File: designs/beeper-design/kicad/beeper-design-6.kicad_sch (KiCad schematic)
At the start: 24 parts, among them U13 CSD75207W15, U3 BQ51003YFPR, U5 FH19C-6S-0.5SH(10)

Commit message: another export
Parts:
- removed C14: 2.2u, beeper-design:Pkg0201_25, symbol my_capacitor_7
- removed C15: 470n, beeper-design:Pkg0201_21, symbol my_capacitor_5
- removed C16: 470n, beeper-design:Pkg0201_31, symbol my_capacitor_10
- removed C17: 22n, beeper-design:Pkg0201_45, symbol my_capacitor_18
- removed C18: 22n, beeper-design:Pkg0201_9, symbol my_capacitor_2
- removed C19: 10n, beeper-design:Pkg0201_18, symbol my_capacitor_4
- removed C20: 10n, beeper-design:Pkg0201_30, symbol my_capacitor_9
- removed C21: 270p, beeper-design:Pkg0201_43, symbol my_capacitor_16
- removed C22: 10n, beeper-design:Pkg0201_7, symbol my_capacitor
- removed C23: 10u, beeper-design:Pkg0402_2, symbol C105225_2
- removed C24: 4.7u, beeper-design:Pkg0402_6, symbol C23733_1
- removed C25: 4.7u, beeper-design:Pkg0402_4, symbol C23733
- removed R2: 845R, beeper-design:Pkg0201_36, symbol my_resistor_10
- removed R3: 196R, beeper-design:Pkg0201_2, symbol C138167
- removed R4: 20K, beeper-design:Pkg0201_12, symbol my_resistor_3
- removed R5: 10K, beeper-design:Pkg0201_22, symbol my_resistor_7
- removed R6: 10K, beeper-design:Pkg0201_34, symbol my_resistor_9
- removed R7: 10K, beeper-design:Pkg0201, symbol my_resistor_12
- removed R8: 1K, beeper-design:Pkg0201_11, symbol my_resistor_2
- removed U13: CSD75207W15, beeper-design:LP_6, symbol CSD75207W15
- added C14: 2.2u, beeper-design:Pkg0201_2, symbol C335106
- added C15: 2.2u, beeper-design:Pkg0201_51, symbol C335106_35
- added C16: 2.2u, beeper-design:Pkg0201_12, symbol C335106_10
- added C17: 2.2u, beeper-design:Pkg0201_25, symbol C335106_18
- added C18: 2.2u, beeper-design:Pkg0201_37, symbol C335106_26
- added C19: 2.2u, beeper-design:Pkg0201_49, symbol C335106_33
- added C20: 2.2u, beeper-design:Pkg0201_10, symbol C335106_8
- added C21: 2.2u, beeper-design:Pkg0201_23, symbol C335106_16
- added C22: 2.2u, beeper-design:Pkg0201_35, symbol C335106_25
- added C23: 2.2u, beeper-design:Pkg0201_48, symbol C335106_32
- added C24: 2.2u, beeper-design:Pkg0201_7, symbol C335106_5
- added C25: 2.2u, beeper-design:Pkg0201_22, symbol C335106_15
- added R2: 845R, beeper-design:Pkg0201_15, symbol my_resistor_1
- added R3: 10K, beeper-design:Pkg0201_14, symbol my_resistor
- added R4: 20K, beeper-design:Pkg0201_41, symbol my_resistor_10
- added R5: 10K, beeper-design:Pkg0201, symbol my_resistor_14
- added R6: 196R, beeper-design:Pkg0201_28, symbol C138167
- added R7: 10K, beeper-design:Pkg0201_26, symbol my_resistor_5
- added R8: 1K, beeper-design:Pkg0201_38, symbol my_resistor_8
- U3: footprint beeper-design:LP_7 -> beeper-design:LP_6
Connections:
- net VDD1P8 is gone; now on net VBUS: U3.D1 (OUT), U3.D2 (OUT), U3.D3 (OUT), U3.D4 (OUT)
- net GND: now also C14.1, C23.1, C24.1, C25.1, R3.2, R5.2, R6.2, R7.2, R8.2
- net VBUS: now also C14.2, C25.2
- net mcu_mcu-wpwr0_gpio: now also R5.1
- net mcu_mcu-wpwr1_gpio: now also R3.1
- net mcu_mcu-wpwr3_gpio: now also R7.1
- net at U3.B3 (AC1), U3.B4 (AC1): now also C15.1, C17.1, C19.1, C21.2, C22.2
- net at U3.C4 (BOOT1): now also C19.2
- net at TP14.p, U3.B1 (AC2), U3.B2 (AC2): now also C16.1, C18.1, C20.1, C21.1
- net at U3.C1 (BOOT2): now also C20.2
- net at U3.C2 (RECT), U3.C3 (RECT): now also C23.2, C24.2, R4.2
- net at U3.G1 (ILIM): now also R2.1
- net at U3.F2 (FOD): now also R2.2, R4.1, R6.1
- net at U3.E3 (CLAMP1): now also C15.2
- net at U3.E1 (COMM2): now also C18.2
- net at U3.E2 (CLAMP2): now also C16.2
- net at U3.E4 (COMM1): now also C17.2
- net at U3.G4 (AD): now also R8.1
- net at TP13.p: now also C22.1

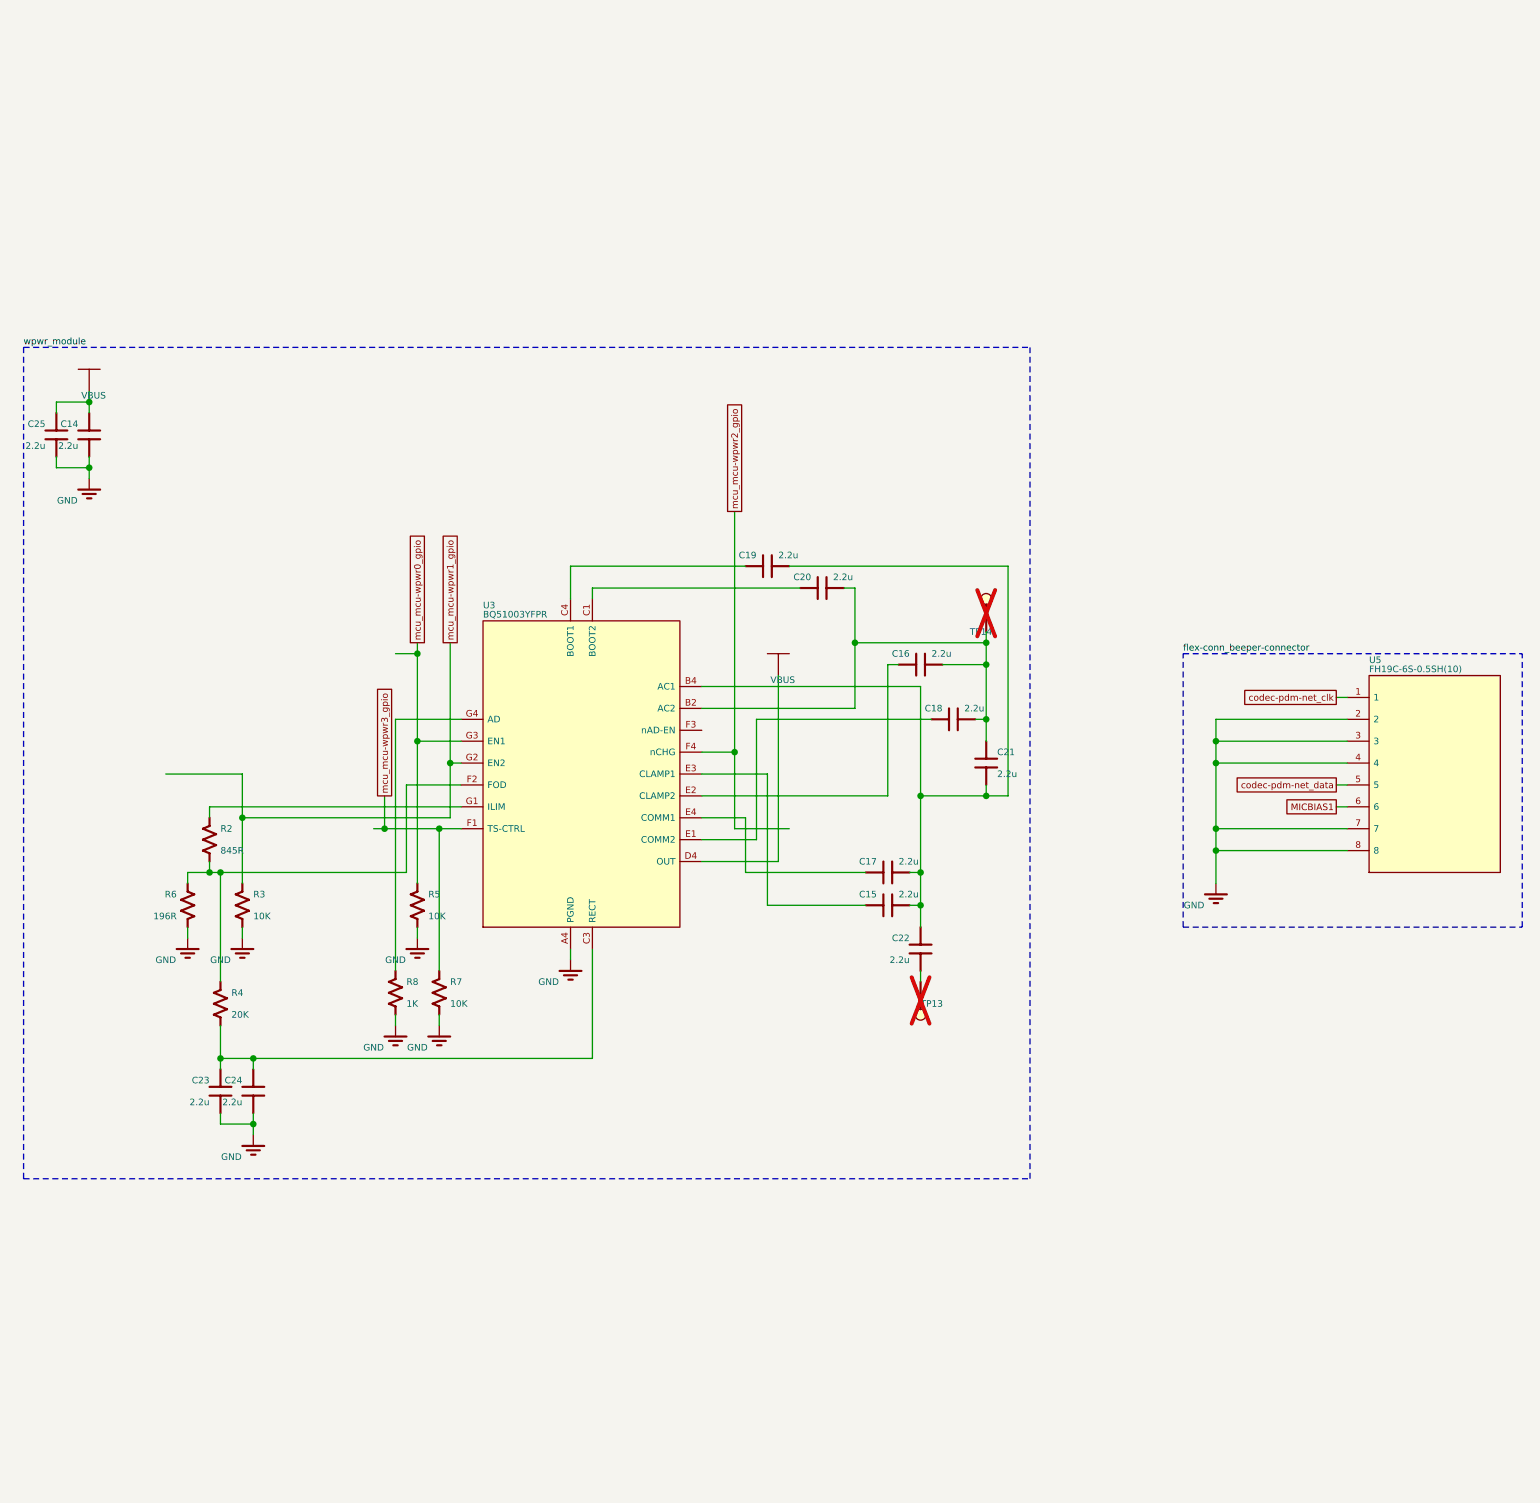
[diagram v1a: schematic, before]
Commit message: crash with new usb connector
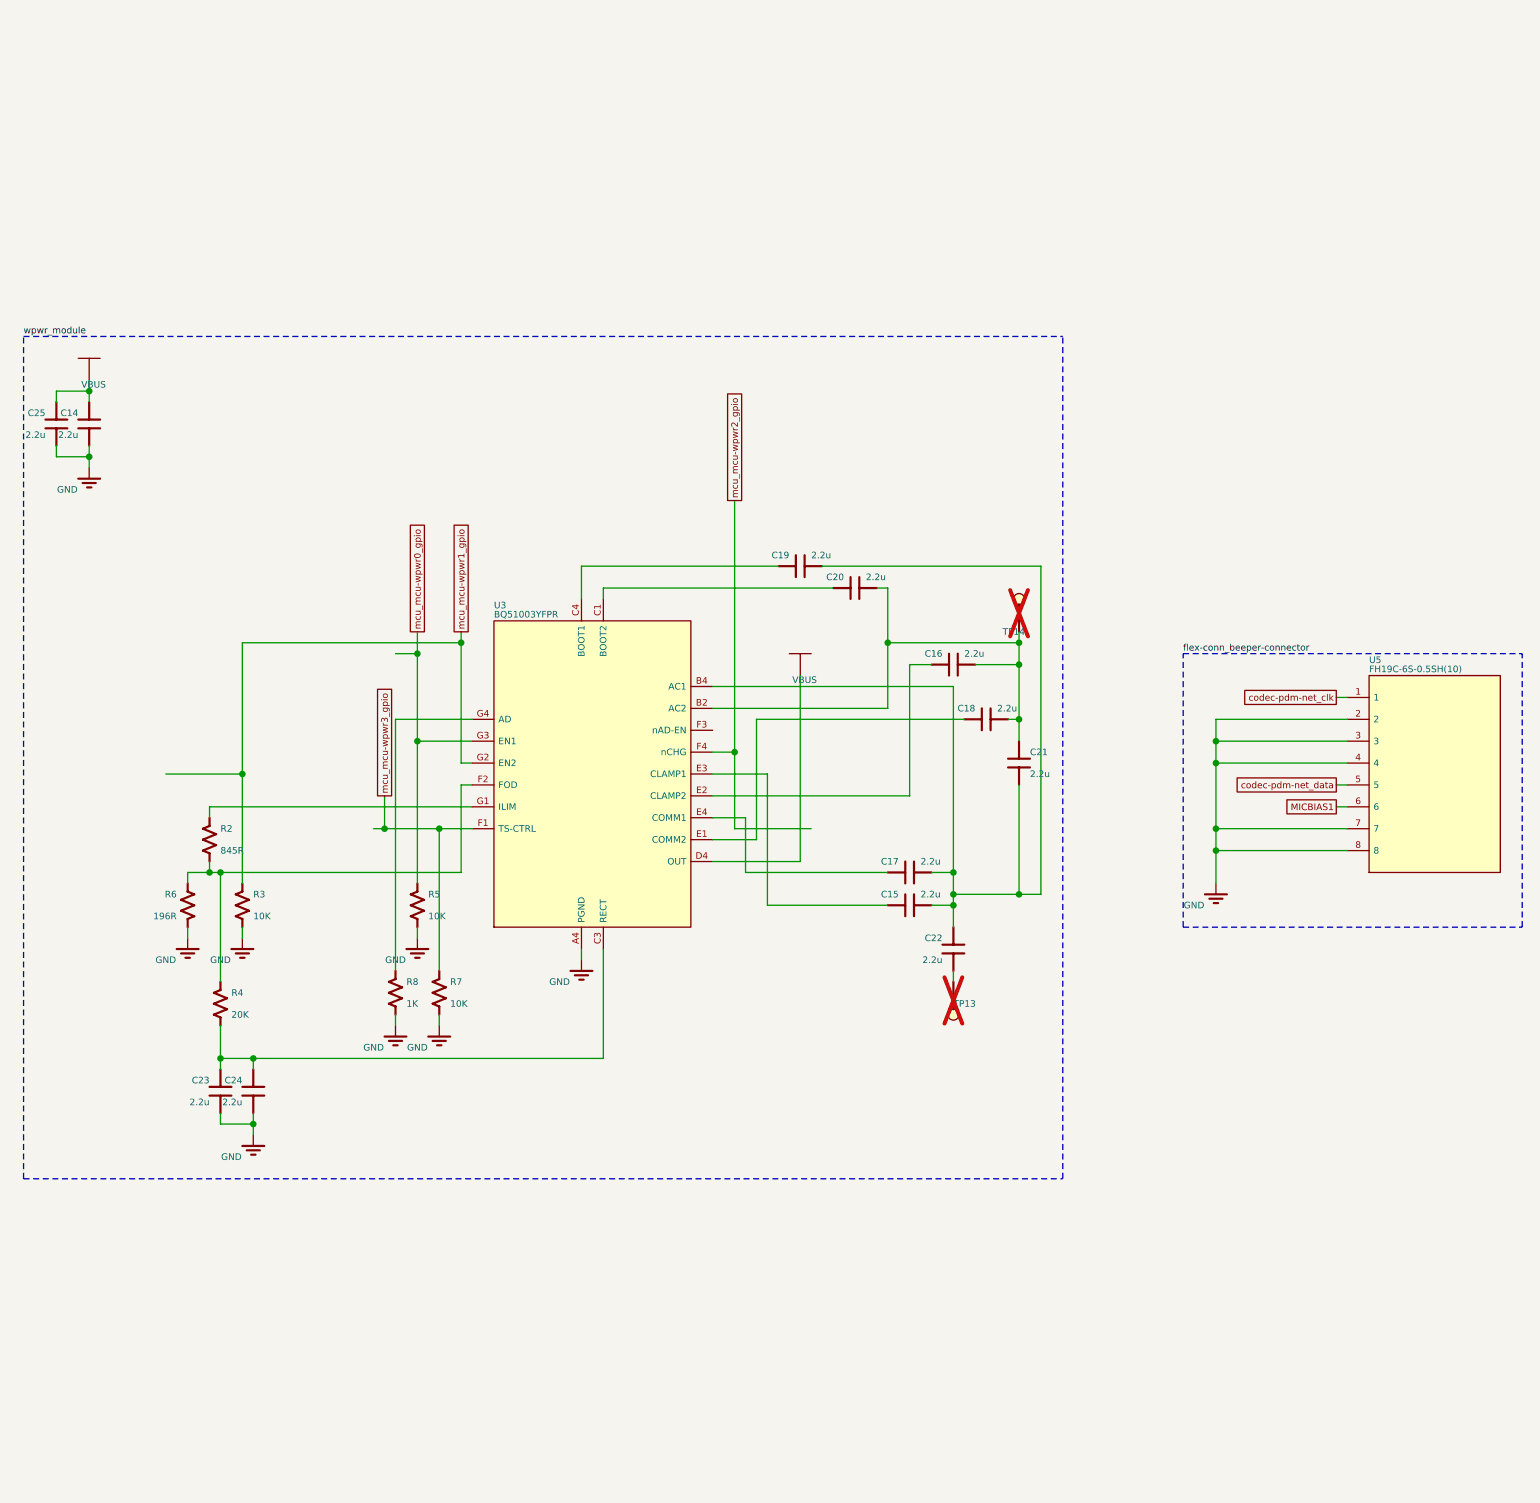
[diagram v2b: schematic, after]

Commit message: new export
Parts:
- removed C14: 2.2u, beeper-design:Pkg0201_2, symbol C335106
- removed C15: 2.2u, beeper-design:Pkg0201_51, symbol C335106_35
- removed C16: 2.2u, beeper-design:Pkg0201_12, symbol C335106_10
- removed C17: 2.2u, beeper-design:Pkg0201_25, symbol C335106_18
- removed C18: 2.2u, beeper-design:Pkg0201_37, symbol C335106_26
- removed C19: 2.2u, beeper-design:Pkg0201_49, symbol C335106_33
- removed C20: 2.2u, beeper-design:Pkg0201_10, symbol C335106_8
- removed C21: 2.2u, beeper-design:Pkg0201_23, symbol C335106_16
- removed C22: 2.2u, beeper-design:Pkg0201_35, symbol C335106_25
- removed C23: 2.2u, beeper-design:Pkg0201_48, symbol C335106_32
- removed C24: 2.2u, beeper-design:Pkg0201_7, symbol C335106_5
- removed C25: 2.2u, beeper-design:Pkg0201_22, symbol C335106_15
- removed R2: 845R, beeper-design:Pkg0201_15, symbol my_resistor_1
- removed R4: 20K, beeper-design:Pkg0201_41, symbol my_resistor_10
- removed R7: 10K, beeper-design:Pkg0201_26, symbol my_resistor_5
- removed R8: 1K, beeper-design:Pkg0201_38, symbol my_resistor_8
- added C14: 2.2u, beeper-design:Pkg0201, symbol C335106_35
- added C15: 2.2u, beeper-design:Pkg0201_50, symbol C335106_31
- added C16: 2.2u, beeper-design:Pkg0201_9, symbol C335106_7
- added C17: 2.2u, beeper-design:Pkg0201_22, symbol C335106_14
- added C18: 2.2u, beeper-design:Pkg0201_36, symbol C335106_22
- added C19: 2.2u, beeper-design:Pkg0201_49, symbol C335106_30
- added C20: 2.2u, beeper-design:Pkg0201_7, symbol C335106_5
- added C21: 2.2u, beeper-design:Pkg0201_20, symbol C335106_12
- added C22: 2.2u, beeper-design:Pkg0201_33, symbol C335106_20
- added C23: 2.2u, beeper-design:Pkg0201_48, symbol C335106_29
- added C24: 2.2u, beeper-design:Pkg0201_6, symbol C335106_4
- added C25: 2.2u, beeper-design:Pkg0201_18, symbol C335106_11
- added R2: 845R, beeper-design:Pkg0201_15, symbol my_resistor_3
- added R4: 20K, beeper-design:Pkg0201_40, symbol my_resistor_11
- added R7: 10K, beeper-design:Pkg0201_23, symbol my_resistor_6
- added R8: 1K, beeper-design:Pkg0201_38, symbol my_resistor_10
- R3: footprint beeper-design:Pkg0201_14 -> beeper-design:Pkg0201_10
- R5: footprint beeper-design:Pkg0201 -> beeper-design:Pkg0201_52
- R6: footprint beeper-design:Pkg0201_28 -> beeper-design:Pkg0201_27
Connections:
- net GND: now also C14.1, C23.1, C24.1, C25.1, R7.2, R8.2
- net VBUS: now also C14.2, C25.2
- net mcu_mcu-wpwr3_gpio: now also R7.1
- net at TP14.p, U3.B1 (AC2), U3.B2 (AC2): now also C16.1, C18.1, C20.1, C21.1
- net at U3.C1 (BOOT2): now also C20.2
- net at U3.C2 (RECT), U3.C3 (RECT): now also C23.2, C24.2, R4.2
- net at R6.1, U3.F2 (FOD): now also R2.2, R4.1
- net at U3.E1 (COMM2): now also C18.2
- net at U3.B3 (AC1), U3.B4 (AC1): now also C15.1, C17.1, C19.1, C21.2, C22.2
- net at U3.C4 (BOOT1): now also C19.2
- net at U3.E2 (CLAMP2): now also C16.2
- net at U3.E3 (CLAMP1): now also C15.2
- net at U3.E4 (COMM1): now also C17.2
- net at U3.G1 (ILIM): now also R2.1
- net at U3.G4 (AD): now also R8.1
- net at TP13.p: now also C22.1
